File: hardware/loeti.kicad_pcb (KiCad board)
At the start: 4 copper layers, 60 x 80 mm, 62 parts, among them J1 USB_C_Receptacle_USB2.0, J2 20021112-00014T1LF, J3 AudioJack3, Q1 BC817, Q2 BC817, Q3 BC807, Q4 Si4825DDY, DMG4435SSS, IRF939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, SW1 key2, SW2 SW_SPST, SW3 SW_SPST, U1 AP2204R-3.3, U2 STUSB4500QTR, U4 EA_DOGS104B-A, U5 STM32F030K6Tx, U6 ADS1118IDGS, U7 INA301A, U8 ASSR-1218, U9 ASSR-1218

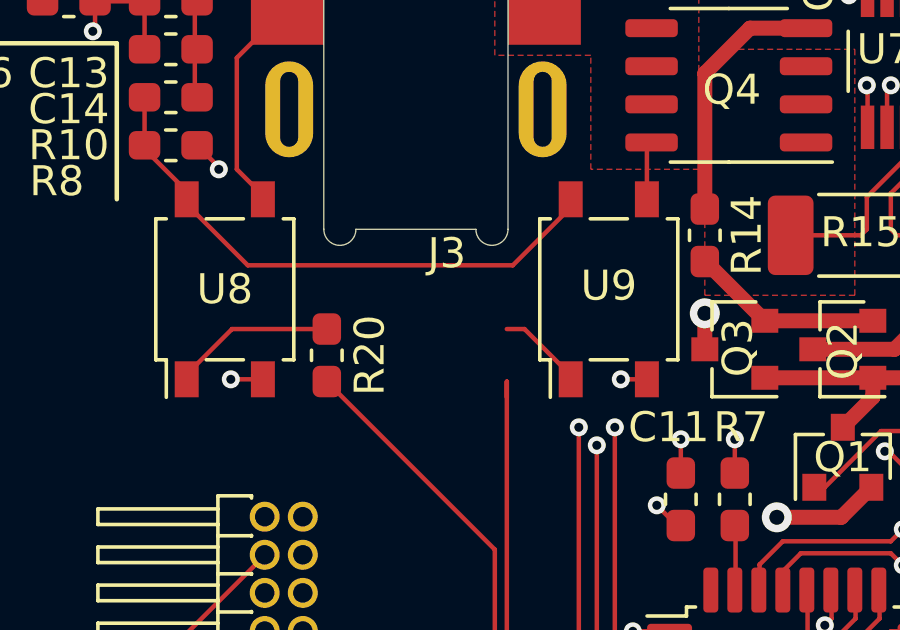
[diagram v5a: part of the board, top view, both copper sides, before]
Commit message: missing footprint
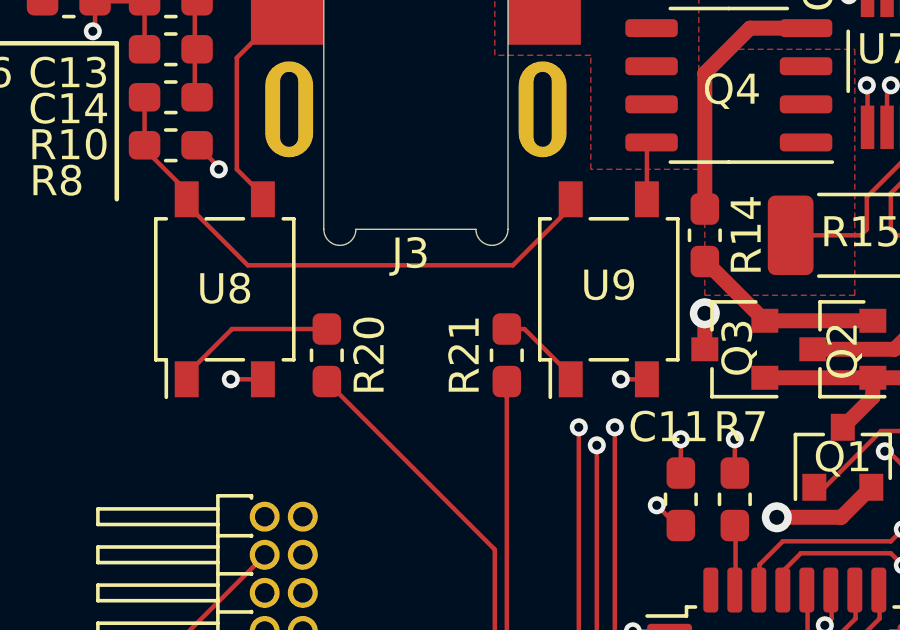
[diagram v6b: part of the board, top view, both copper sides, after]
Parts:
- added R21: 470, Resistor_SMD:R_0603_1608Metric_Pad1.05x0.95mm_HandSolder, F.Cu at (79.4, 58.7)
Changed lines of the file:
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@@
     (tracks 516)
     (zones 0)
-    (modules 62)
+    (modules 63)
     (nets 48)
   )
@@
     (add_net "Net-(C3-Pad2)")
     (add_net "Net-(C4-Pad1)")
+    (add_net "Net-(J1-PadA6)")
+    (add_net "Net-(J1-PadA7)")
+    (add_net "Net-(J1-PadA8)")
+    (add_net "Net-(J1-PadB6)")
+    (add_net "Net-(J1-PadB7)")
+    (add_net "Net-(J1-PadB8)")
+    (add_net "Net-(J2-Pad1)")
+    (add_net "Net-(J2-Pad10)")
+    (add_net "Net-(J2-Pad2)")
+    (add_net "Net-(J2-Pad9)")
     (add_net "Net-(Q1-Pad1)")
     (add_net "Net-(Q1-Pad3)")
@@
     (add_net "Net-(SW2-Pad1)")
     (add_net "Net-(SW3-Pad1)")
+    (add_net "Net-(U2-Pad11)")
+    (add_net "Net-(U2-Pad14)")
+    (add_net "Net-(U2-Pad15)")
+    (add_net "Net-(U2-Pad16)")
+    (add_net "Net-(U2-Pad17)")
+    (add_net "Net-(U2-Pad20)")
+    (add_net "Net-(U2-Pad3)")
+    (add_net "Net-(U2-Pad9)")
+    (add_net "Net-(U4-Pad1)")
+    (add_net "Net-(U4-Pad10)")
+    (add_net "Net-(U4-Pad2)")
+    (add_net "Net-(U4-Pad9)")
+    (add_net "Net-(U5-Pad11)")
+    (add_net "Net-(U5-Pad14)")
+    (add_net "Net-(U6-Pad4)")
+    (add_net "Net-(U6-Pad5)")
     (add_net PD_ALERT_INT)
     (add_net PD_RST)
@@
     (add_net SWCLK)
     (add_net SWDIO)
+    (add_net SWO)
     (add_net T+)
     (add_net VCP_RX)
     (add_net VCP_TX)
+  )
+  (module Resistor_SMD:R_0603_1608Metric_Pad1.05x0.95mm_HandSolder (layer F.Cu)
+    (at 79.4 58.7 270)
+    (descr "Resistor SMD 0603 (1608 Metric), square (rectangular) end terminal, IPC_7351 nominal with elongated pad for handsoldering. (Body size source: http://www.tortai-tech.com/upload/download/2011102023233369053.pdf), generated with kicad-footprint-generator")
+    (tags "resistor handsolder")
+    (attr smd)
+    (fp_text reference R21 (at 0 1.4 90) (layer F.SilkS)
+      (effects (font (size 1 1) (thickness 0.15)))
+    )
+    (fp_text value 470 (at 0 1.43 90) (layer F.Fab)
+      (effects (font (size 1 1) (thickness 0.15)))
+    )
+    (fp_text user %R (at 0 0 90) (layer F.Fab)
+      (effects (font (size 0.4 0.4) (thickness 0.06)))
+    )
+    (fp_line (start 1.65 0.73) (end -1.65 0.73) (layer F.CrtYd) (width 0.05))
+    (fp_line (start 1.65 -0.73) (end 1.65 0.73) (layer F.CrtYd) (width 0.05))
+    (fp_line (start -1.65 -0.73) (end 1.65 -0.73) (layer F.CrtYd) (width 0.05))
+    (fp_line (start -1.65 0.73) (end -1.65 -0.73) (layer F.CrtYd) (width 0.05))
+    (fp_line (start -0.171267 0.51) (end 0.171267 0.51) (layer F.SilkS) (width 0.12))
+    (fp_line (start -0.171267 -0.51) (end 0.171267 -0.51) (layer F.SilkS) (width 0.12))
+    (fp_line (start 0.8 0.4) (end -0.8 0.4) (layer F.Fab) (width 0.1))
+    (fp_line (start 0.8 -0.4) (end 0.8 0.4) (layer F.Fab) (width 0.1))
+    (fp_line (start -0.8 -0.4) (end 0.8 -0.4) (layer F.Fab) (width 0.1))
+    (fp_line (start -0.8 0.4) (end -0.8 -0.4) (layer F.Fab) (width 0.1))
+    (pad 2 smd roundrect (at 0.875 0 270) (size 1.05 0.95) (layers F.Cu F.Paste F.Mask) (roundrect_rratio 0.25)
+      (net 39 SEL_TC_1))
+    (pad 1 smd roundrect (at -0.875 0 270) (size 1.05 0.95) (layers F.Cu F.Paste F.Mask) (roundrect_rratio 0.25)
+      (net 40 "Net-(R21-Pad1)"))
+    (model ${KISYS3DMOD}/Resistor_SMD.3dshapes/R_0603_1608Metric.wrl
+      (at (xyz 0 0 0))
+      (scale (xyz 1 1 1))
+      (rotate (xyz 0 0 0))
+    )
   )
   (module Package_QFP:LQFP-32_7x7mm_P0.8mm (layer F.Cu)
@@
   (module custom:CUI_SJ-3502-SMT (layer F.Cu)
     (at 76.37 47.85 270)
-    (fp_text reference J3 (at 7.45 -1.03) (layer F.SilkS)
+    (fp_text reference J3 (at 7.4627 0.1758) (layer F.SilkS)
       (effects (font (size 1.00148 1.00148) (thickness 0.15)))
     )

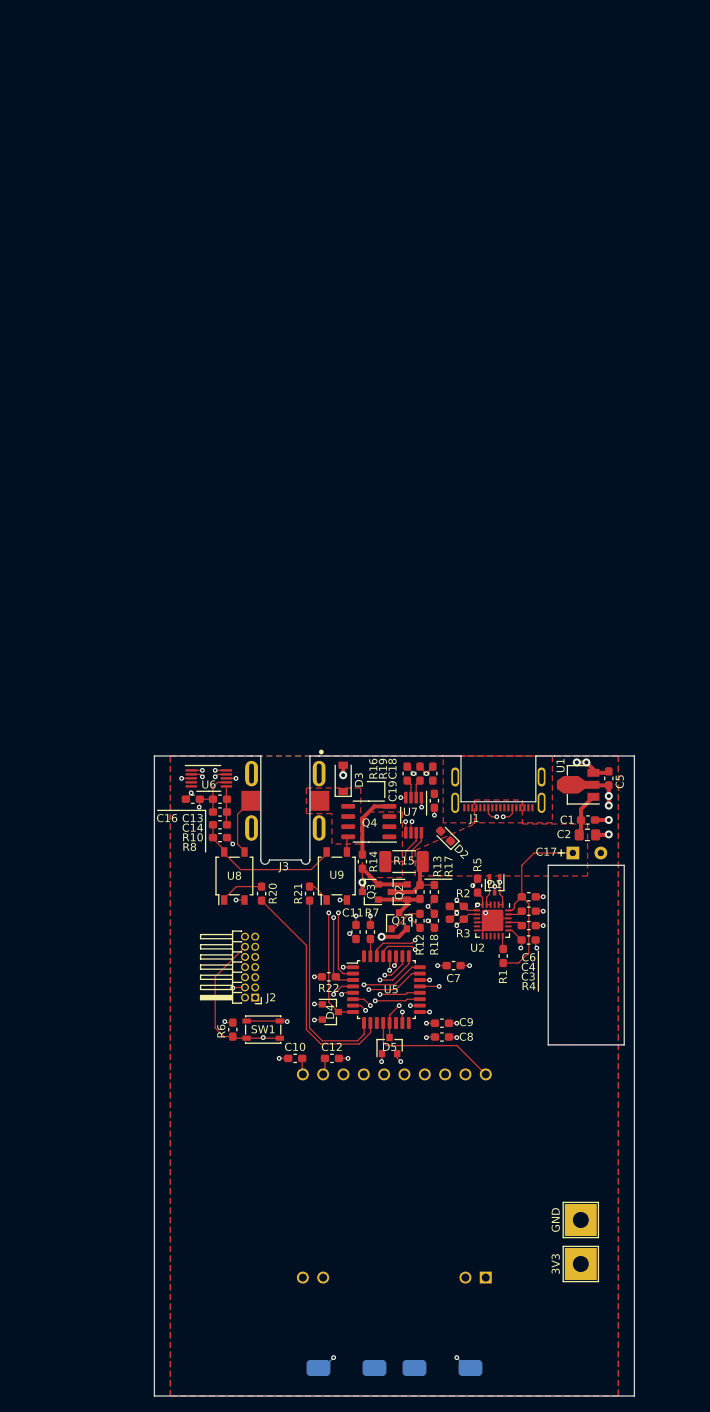
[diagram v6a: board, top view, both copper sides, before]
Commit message: preliminary layout
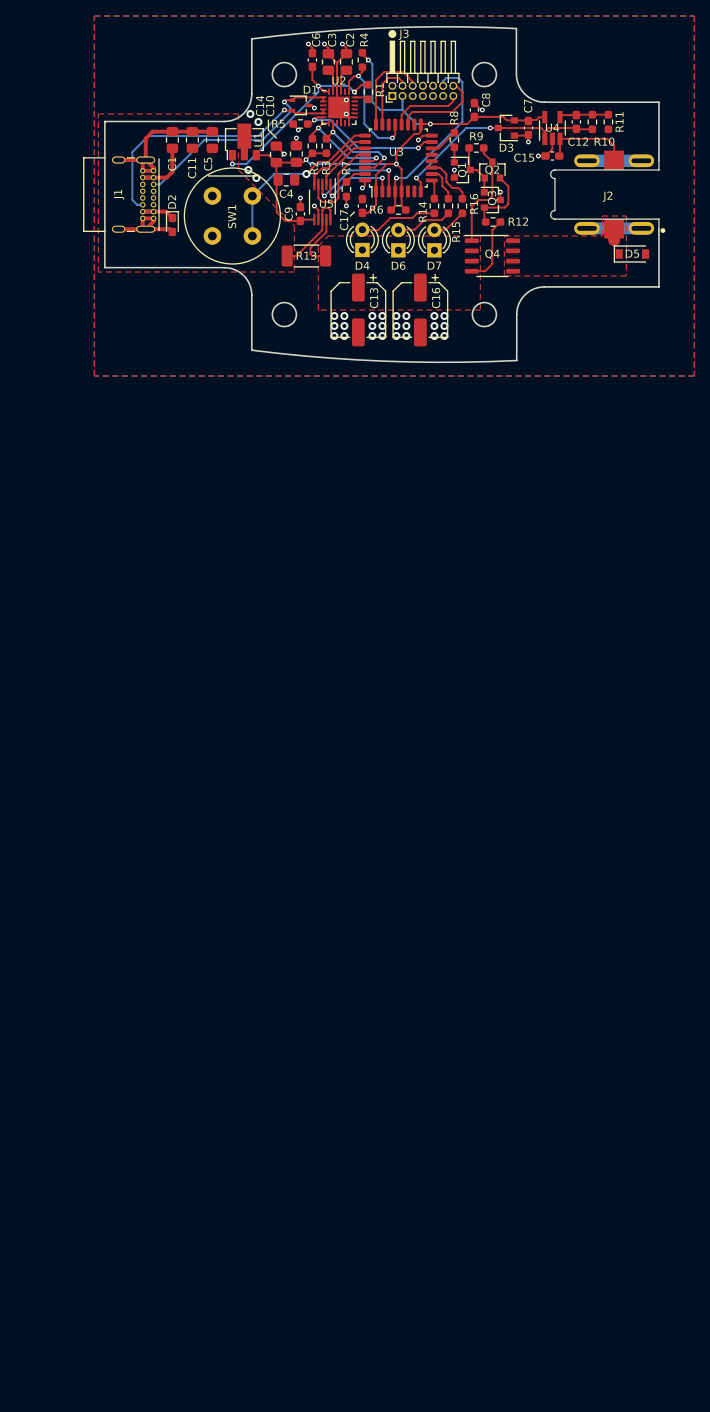
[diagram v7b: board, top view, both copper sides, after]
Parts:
- removed C18, C19: 0.1μF, Capacitor_SMD:C_0603_1608Metric_Pad1.05x0.95mm_HandSolder
- removed R17, R19, R22: 10k, Resistor_SMD:R_0603_1608Metric_Pad1.05x0.95mm_HandSolder
- removed R18: 1k, Resistor_SMD:R_0603_1608Metric_Pad1.05x0.95mm_HandSolder
- removed R20, R21: 470, Resistor_SMD:R_0603_1608Metric_Pad1.05x0.95mm_HandSolder
- removed SW2, SW3: SW_SPST, custom:Omron-B3AL
- removed TP2: GND, TestPoint:TestPoint_THTPad_4.0x4.0mm_Drill2.0mm
- removed TP3: 3V3, TestPoint:TestPoint_THTPad_4.0x4.0mm_Drill2.0mm
- removed U6: ADS1118IDGS, Package_SO:VSSOP-10_3x3mm_P0.5mm
- removed U7: INA301A, Package_SO:VSSOP-8_3.0x3.0mm_P0.65mm
- removed U8, U9: ASSR-1218, Package_SO:SO-4_4.4x4.3mm_P2.54mm
- added C15: 0.1μF, Capacitor_SMD:C_0603_1608Metric_Pad1.08x0.95mm_HandSolder, F.Cu at (109.8, -33.5)
- added D6: LED, LED_THT:LED_D3.0mm, F.Cu at (90.5, -21.7)
- added D7: LED, LED_THT:LED_D3.0mm, F.Cu at (95.0, -21.7)
- added R11: 1k, Resistor_SMD:R_0603_1608Metric_Pad0.98x0.95mm_HandSolder, F.Cu at (116.8, -37.8)
- added R9: 1k, Resistor_SMD:R_0603_1608Metric_Pad0.98x0.95mm_HandSolder, F.Cu at (100.2, -34.5)
- added U3: STM32F030K6Tx, Package_QFP:LQFP-32_7x7mm_P0.8mm, F.Cu at (90.5, -33.2)
- C1, C10, C11, C14, C3, C4, C5: footprint Capacitor_SMD:C_0603_1608Metric_Pad1.05x0.95mm_HandSolder -> Capacitor_SMD:C_0805_2012Metric_Pad1.18x1.45mm_HandSolder
- C12: value 1μF 25V -> 0.1μF; footprint Capacitor_SMD:C_0603_1608Metric_Pad1.05x0.95mm_HandSolder -> Capacitor_SMD:C_0603_1608Metric_Pad1.08x0.95mm_HandSolder
- C13, C16: value 0.1μF -> CP; footprint Capacitor_SMD:C_0603_1608Metric_Pad1.05x0.95mm_HandSolder -> Capacitor_SMD:CP_Elec_6.3x5.9
- C17: value EEU-FR1V471L -> 0.1μF; footprint custom:CP_Radial_D8.0mm_P3.50mm_HOR -> Capacitor_SMD:C_0603_1608Metric_Pad1.08x0.95mm_HandSolder
- C2: value 4.7μF 25V -> 1μF 25V; footprint Capacitor_SMD:C_0805_2012Metric_Pad1.15x1.40mm_HandSolder -> Capacitor_SMD:C_0805_2012Metric_Pad1.18x1.45mm_HandSolder
- C6, C7, C8, C9: footprint Capacitor_SMD:C_0603_1608Metric_Pad1.05x0.95mm_HandSolder -> Capacitor_SMD:C_0603_1608Metric_Pad1.08x0.95mm_HandSolder
- D3: value D_Schottky -> BAT54S; footprint Diode_SMD:D_SOD-123 -> Package_TO_SOT_SMD:SOT-23
- D4: value BAT54S -> LED; footprint Package_TO_SOT_SMD:SOT-23 -> LED_THT:LED_D3.0mm
- D5: value BAT54S -> D_Schottky; footprint Package_TO_SOT_SMD:SOT-23 -> Diode_SMD:D_SOD-123
- J1: footprint custom:CX90M-16P -> Connector_USB:USB_C_Receptacle_GCT_USB4085
- J2: value 20021112-00014T1LF -> AudioJack3; footprint Connector_PinHeader_1.27mm:PinHeader_2x07_P1.27mm_Horizontal -> custom:CUI_SJ-3502-SMT
- J3: value AudioJack3 -> 20021112-00014T1LF; footprint custom:CUI_SJ-3502-SMT -> Connector_PinHeader_1.27mm:PinHeader_2x07_P1.27mm_Horizontal
- R1, R2, R3, R4, R5, R6, R7: footprint Resistor_SMD:R_0603_1608Metric_Pad1.05x0.95mm_HandSolder -> Resistor_SMD:R_0603_1608Metric_Pad0.98x0.95mm_HandSolder
- R10: value 47 -> 220k; footprint Resistor_SMD:R_0603_1608Metric_Pad1.05x0.95mm_HandSolder -> Resistor_SMD:R_0603_1608Metric_Pad0.98x0.95mm_HandSolder
- R12: value 1k -> 20; footprint Resistor_SMD:R_0603_1608Metric_Pad1.05x0.95mm_HandSolder -> Resistor_SMD:R_0603_1608Metric_Pad0.98x0.95mm_HandSolder
- R13: value 1k -> WSLP2010R0100FEA; footprint Resistor_SMD:R_0603_1608Metric_Pad1.05x0.95mm_HandSolder -> Resistor_SMD:R_2010_5025Metric_Pad1.40x2.65mm_HandSolder
- R14: value 20 -> 1k; footprint Resistor_SMD:R_0603_1608Metric_Pad1.05x0.95mm_HandSolder -> Resistor_SMD:R_0603_1608Metric_Pad0.98x0.95mm_HandSolder
- R15: value WSLP2010R0100FEA -> 1k; footprint Resistor_SMD:R_2010_5025Metric_Pad1.52x2.65mm_HandSolder -> Resistor_SMD:R_0603_1608Metric_Pad0.98x0.95mm_HandSolder
- R16: value 25k -> 1k; footprint Resistor_SMD:R_0603_1608Metric_Pad1.05x0.95mm_HandSolder -> Resistor_SMD:R_0603_1608Metric_Pad0.98x0.95mm_HandSolder
- R8: value 1M -> 1k; footprint Resistor_SMD:R_0603_1608Metric_Pad1.05x0.95mm_HandSolder -> Resistor_SMD:R_0603_1608Metric_Pad0.98x0.95mm_HandSolder
- SW1: value key2 -> D6R; footprint Button_Switch_SMD:SW_SPST_PTS810 -> custom:D6R
- U4: value EA_DOGS104B-A -> TLV333-DBV; footprint Display:EA_DOGS104X-A -> Package_TO_SOT_SMD:SOT-23-5_HandSoldering; moved to F.Cu
- U5: value STM32F030K6Tx -> INA239; footprint Package_QFP:LQFP-32_7x7mm_P0.8mm -> Package_SO:VSSOP-10_3x3mm_P0.5mm
- moved U4 143.9 mm to (109.8, -37.0)
- moved C12 121.0 mm to (112.8, -37.8), turned to 90 degrees
- moved C8 115.9 mm to (100.0, -39.2), turned to 90 degrees
- moved C10 113.1 mm to (77.8, -33.8), turned to 90 degrees
- moved R4 111.9 mm to (86.0, -45.5), turned to 90 degrees
- moved C3 110.8 mm to (81.8, -45.2), turned to 90 degrees
- moved J2 109.6 mm to (116.7, -28.7)
- moved R1 109.3 mm to (86.8, -41.5), turned to 90 degrees
- moved C6 108.0 mm to (79.8, -45.5), turned to 270 degrees
- moved C7 105.1 mm to (106.8, -37.0), turned to 270 degrees
- moved R6 104.5 mm to (90.5, -26.8), turned to 180 degrees
- moved D5 103.5 mm to (119.8, -21.2), turned to 0 degrees
- moved U2 103.4 mm to (83.1, -39.6), turned to 0 degrees
- moved C9 102.7 mm to (78.2, -26.2), turned to 90 degrees
- moved SW1 101.8 mm to (69.8, -26.0), turned to 270 degrees
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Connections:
- C10 pad 1: Net-(C10-Pad1) -> +3V3
- C11 pad 1: +3V3 -> SHUNT+
- C12 pad 1: +3V3 -> ADC_IN2
- C12 pad 2: HEATER- -> Net-(C12-Pad2)
- C13 pad 1: HEATER- -> SHUNT-
- C13 pad 2: Net-(C13-Pad2) -> HEATER-
- C14 pad 1: HEATER- -> +3V3
- C14 pad 2: Net-(C13-Pad2) -> HEATER-
- C16 pad 1: +3V3 -> SHUNT-
- C17 pad 1: SHUNT+ -> +3V3
- C2 pad 1: SHUNT+ -> HEATER-
- C2 pad 2: HEATER- -> Net-(C2-Pad2)
- C3 pad 1: HEATER- -> Net-(C3-Pad1)
- C3 pad 2: Net-(C3-Pad2) -> HEATER-
- C4 pad 1: Net-(C4-Pad1) -> +3V3
- C5 pad 1: +3V3 -> SHUNT+
- D3 pad 1: HEATER+ -> HEATER-
- D3 pad 2: HEATER- -> +3V3
- D4 pad 2: +3V3 -> Net-(D4-Pad2)
- D5 pad 1: HEATER- -> HEATER+
- D5 pad 2: +3V3 -> HEATER-
- Q2 pad 3: SHUNT+ -> SHUNT-
- R10 pad 1: Net-(R10-Pad1) -> ADC_IN2
- R10 pad 2: Net-(C13-Pad2) -> Net-(C12-Pad2)
- R12 pad 1: PWM -> Net-(Q2-Pad2)
- R12 pad 2: Net-(Q1-Pad1) -> Net-(Q4-Pad4)
- R13 pad 1: Net-(Q1-Pad3) -> SHUNT+
- R13 pad 2: SHUNT+ -> SHUNT-
- R14 pad 1: Net-(Q2-Pad2) -> Net-(D4-Pad2)
- R14 pad 2: Net-(Q4-Pad4) -> LED0
- R15 pad 1: SHUNT+ -> Net-(D6-Pad2)
- R15 pad 2: SHUNT- -> LED1
- R16 pad 1: HEATER- -> Net-(D7-Pad2)
- R16 pad 2: CUR_LIMIT -> LED2
- R8 pad 1: Net-(R10-Pad1) -> PWM
- R8 pad 2: +3V3 -> Net-(Q1-Pad1)
- SW1 pad 1: NRST -> SW
- SW1 pad 2: HEATER- -> SW
- U2 pad 21: Net-(C3-Pad2) -> Net-(C2-Pad2)
- U2 pad 23: Net-(C4-Pad1) -> Net-(C3-Pad1)
- U4 pad 1: (no net) -> ADC_IN2
- U4 pad 2: (no net) -> HEATER-
- U5 pad 1: +3V3 -> CURR_CS
- U5 pad 10: SEL_TC_0 -> SHUNT+
- U5 pad 2: CUR_RESET -> SPI1_MISO
- U5 pad 3: CUR_NALERT -> CURR_ALERT
- U5 pad 4: NRST -> SPI1_MOSI
- U5 pad 5: +3V3 -> SPI1_SCK
- U5 pad 6: Net-(SW2-Pad1) -> +3V3
- U5 pad 7: Net-(SW3-Pad1) -> HEATER-
- U5 pad 8: ADC_IN2 -> SHUNT+
- U5 pad 9: SEL_TC_1 -> SHUNT-
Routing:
- net +3V3: track 28.5 -> 87.4 mm, vias 20 -> 4
- net SPI1_SCK: track 64.4 -> 9.14 mm, vias 2 -> 0
- net Net-(SW2-Pad1): track 53.2 -> 0.00 mm, vias 2 -> 0
- net SPI1_MISO: track 59.2 -> 7.30 mm, vias 2 -> 0
- net Net-(SW3-Pad1): track 49.3 -> 0.00 mm, vias 2 -> 0
- net SPI1_NSS1: track 44.7 -> 0.00 mm, vias 2 -> 0
- net SPI1_MOSI: track 55.3 -> 11.9 mm, vias 2 -> 0
- net SEL_TC_0: track 29.0 -> 0.00 mm
- net CUR_NALERT: track 28.3 -> 0.00 mm, vias 2 -> 0
- net HEATER-: track 56.2 -> 82.9 mm, vias 30 -> 47
- net CUR_RESET: track 26.0 -> 0.00 mm, vias 2 -> 0
- net SEL_TC_1: track 25.7 -> 0.00 mm
- net SW: track 0.00 -> 22.2 mm, vias 0 -> 1
- net ADC_IN7: track 21.7 -> 0.00 mm, vias 2 -> 0
- net SWDIO: track 28.8 -> 8.60 mm, vias 2 -> 0
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- removed copper zone on In1.Cu, net +3V3
- removed copper zone on In2.Cu, net HEATER-
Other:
- board size 60 x 80 mm -> 69.3 x 41.9 mm
- copper layers 4 -> 2
- board text added: "Löti mini"
- board text added: "af 2021 v0.1"
- board text removed: "Löti"
- board text removed: "af 2020"
- board text removed: "hawki edition"
- board text removed: "v4"

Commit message: production version, v5
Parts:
- removed the C10 at (77.8, -33.8)
- removed the C14 at (75.2, -33.7)
- removed the C5 at (67.2, -35.5)
- removed the R12 at (102.3, -25.2)
- removed the R8 at (97.5, -35.5)
- added D11: BZX84Cxx, Package_TO_SOT_SMD:TSOT-23_HandSoldering, F.Cu at (101.2, -38.0)
- added D4: BAS16W, Package_TO_SOT_SMD:SOT-323_SC-70_Handsoldering, F.Cu at (83.5, -25.5)
- added D8: BAS16W, Package_TO_SOT_SMD:SOT-323_SC-70_Handsoldering, F.Cu at (115.0, -37.5)
- added D9: BAS16W, Package_TO_SOT_SMD:SOT-323_SC-70_Handsoldering, F.Cu at (121.5, -37.5)
- added R13: 1k, Resistor_SMD:R_0603_1608Metric_Pad0.98x0.95mm_HandSolder, F.Cu at (100.0, -30.5)
- added R14: 25k, Resistor_SMD:R_0603_1608Metric_Pad0.98x0.95mm_HandSolder, F.Cu at (98.0, -22.5)
- added R15: 1k, Resistor_SMD:R_0603_1608Metric_Pad0.98x0.95mm_HandSolder, F.Cu at (103.5, -32.5)
- added R16: 1M, Resistor_SMD:R_0603_1608Metric_Pad0.98x0.95mm_HandSolder, F.Cu at (110.5, -34.2)
- added R17: 10k, Resistor_SMD:R_0603_1608Metric_Pad0.98x0.95mm_HandSolder, F.Cu at (118.2, -38.2)
- added R20: 20, Resistor_SMD:R_0603_1608Metric_Pad0.98x0.95mm_HandSolder, F.Cu at (108.0, -23.8)
- added R23: 10k, Resistor_SMD:R_0603_1608Metric_Pad0.98x0.95mm_HandSolder, F.Cu at (104.2, -40.8)
- added R24: 10k, Resistor_SMD:R_0603_1608Metric_Pad0.98x0.95mm_HandSolder, F.Cu at (108.0, -29.8)
- added R6: 10k, Resistor_SMD:R_0603_1608Metric_Pad0.98x0.95mm_HandSolder, F.Cu at (89.2, -21.2)
- added R7: 1k, Resistor_SMD:R_0603_1608Metric_Pad0.98x0.95mm_HandSolder, F.Cu at (91.8, -22.2)
- added U4: 74AHC1G08, Package_TO_SOT_SMD:SOT-353_SC-70-5_Handsoldering, F.Cu at (101.5, -34.8)
- added U6: TMP100, Package_TO_SOT_SMD:SOT-23-6_Handsoldering, F.Cu at (84.5, -34.2)
- C10: renamed from C9; value 0.1μF -> 100n
- C11: value 1μF 25V -> 100n; footprint Capacitor_SMD:C_0805_2012Metric_Pad1.18x1.45mm_HandSolder -> Capacitor_SMD:C_0603_1608Metric_Pad1.08x0.95mm_HandSolder
- C12: renamed from C15; value 0.1μF -> 100n
- C13: renamed from C12; value 0.1μF -> 100n
- C14: renamed from C17; value 0.1μF -> 100n
- C3: renamed from C2; value 1μF 25V -> 1u
- C4: renamed from C3; value 1μF 25V -> 1u
- C5: renamed from C1; value 1μF 25V -> 4.7u
- C6: value 0.1μF -> 100n
- C7: renamed from C4; value 1μF 25V -> 4.7u
- C8: renamed from C7; value 0.1μF -> 100n
- C9: renamed from C8; value 0.1μF -> 100n
- D1: footprint Package_TO_SOT_SMD:SOT-323_SC-70 -> Package_TO_SOT_SMD:SOT-323_SC-70_Handsoldering
- D3: value BAT54S -> BAS16W; footprint Package_TO_SOT_SMD:SOT-23 -> Package_TO_SOT_SMD:SOT-323_SC-70_Handsoldering
- D5: renamed from D4; footprint LED_THT:LED_D3.0mm -> LED_THT:LED_D1.8mm_W3.3mm_H2.4mm
- D6, D7: footprint LED_THT:LED_D3.0mm -> LED_THT:LED_D1.8mm_W3.3mm_H2.4mm
- J1: value USB_C_Receptacle_USB2.0 -> GCT USB4105; footprint Connector_USB:USB_C_Receptacle_GCT_USB4085 -> Connector_USB:USB_C_Receptacle_HRO_TYPE-C-31-M-12
- Q1, Q2, Q3: footprint Package_TO_SOT_SMD:SOT-23 -> Package_TO_SOT_SMD:SOT-23_Handsoldering
- R10: renamed from R14; value 1k -> 10k
- R11: renamed from R15; value 1k -> 10k
- R12: renamed from R16; value 1k -> 10k
- R18: renamed from R9; value 1k -> 10k
- U2: renamed from U1; footprint Package_TO_SOT_SMD:SOT-89-3 -> Package_TO_SOT_SMD:SOT-89-3_Handsoldering
- U5: value INA239 -> INA301; footprint Package_SO:VSSOP-10_3x3mm_P0.5mm -> Package_SO:VSSOP-8_3.0x3.0mm_P0.65mm
- moved C11 35.9 mm to (100.0, -28.8), turned to 0 degrees
- moved D7 29.6 mm to (80.5, -47.5), turned to 270 degrees
- moved D6 26.7 mm to (83.8, -47.5), turned to 270 degrees
- moved D5 25.8 mm to (87.0, -47.5), turned to 270 degrees
- moved R19 23.9 mm to (102.8, -18.8)
- moved C10 22.6 mm to (100.0, -32.5), turned to 180 degrees
- moved C14 22.3 mm to (107.1, -34.2), turned to 180 degrees
- moved U5 22.1 mm to (102.5, -22.5), turned to 0 degrees
- moved R12 21.0 mm to (83.5, -42.0), turned to 270 degrees
- moved D3 20.9 mm to (86.5, -25.5), turned to 90 degrees
- moved C8 20.8 mm to (89.0, -26.2)
- moved R11 18.7 mm to (85.2, -42.0), turned to 270 degrees
- moved R10 16.8 mm to (87.0, -42.0), turned to 270 degrees
- moved C9 15.0 mm to (92.5, -26.2), turned to 270 degrees
- moved C6 14.4 mm to (74.0, -32.2), turned to 0 degrees
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- renumbered C13 to C1, C16 to C2, D5 to D10, R13 to R19, R10 to R21, R11 to R22, R7 to R8, R6 to R9, U2 to U1, U4 to U7
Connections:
- C1 pad 1: SHUNT- -> SHUNT+
- C11 pad 1: SHUNT+ -> ADC_IN1
- C13 pad 1: ADC_IN2 -> Net-(C13-Pad1)
- C2 pad 1: SHUNT- -> SHUNT+
- D3 pad 1: HEATER- -> ADC_IN3
- D3 pad 2: +3V3 -> (no net)
- D3 pad 3: ADC_IN2 -> +3V3
- Q2 pad 3: SHUNT- -> SHUNT+
- R18 pad 2: SHUNT- -> SHUNT+
- R21 pad 1: ADC_IN2 -> Net-(C13-Pad1)
- U3 pad 10: LED1 -> (no net)
- U3 pad 11: LED2 -> (no net)
- U3 pad 13: (no net) -> CURR_ALERT
- U3 pad 2: CURR_CS -> SW
- U3 pad 25: SW -> LED0
- U3 pad 26: SPI1_SCK -> LED1
- U3 pad 27: SPI1_MISO -> LED2
- U3 pad 28: SPI1_MOSI -> (no net)
- U3 pad 3: CURR_ALERT -> (no net)
- U3 pad 6: (no net) -> CURR_RESET
- U3 pad 7: (no net) -> ADC_IN1
- U3 pad 9: LED0 -> ADC_IN3
- U5 pad 1: CURR_CS -> +3V3
- U5 pad 2: SPI1_MISO -> Net-(R13-Pad2)
- U5 pad 3: CURR_ALERT -> Net-(R14-Pad2)
- U5 pad 4: SPI1_MOSI -> HEATER-
- U5 pad 5: SPI1_SCK -> CURR_RESET
- U5 pad 6: +3V3 -> CURR_ALERT
- U5 pad 7: HEATER- -> SHUNT-
- U7 pad 1: ADC_IN2 -> Net-(C13-Pad1)
- U7 pad 3: T+ -> Net-(D8-Pad1)
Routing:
- net +3V3: track 87.4 -> 12.9 mm, vias 4 -> 1
- net ADC_IN3: track 0.00 -> 24.7 mm, vias 0 -> 2
- net CURR_RESET: track 0.00 -> 18.7 mm, vias 0 -> 2
- net HEATER-: track 82.9 -> 65.7 mm, vias 47 -> 66
- net Net-(D8-Pad1): track 0.00 -> 15.7 mm
- net ADC_IN2: track 27.8 -> 15.0 mm
- net SHUNT-: track 21.0 -> 8.60 mm
- net SPI1_MOSI: track 11.9 -> 0.00 mm
- net Net-(C13-Pad1): track 0.00 -> 10.8 mm
- net Net-(R13-Pad2): track 0.00 -> 10.7 mm, vias 0 -> 2
- net CURR_CS: track 10.4 -> 0.00 mm, vias 2 -> 0
- net CURR_ALERT: track 13.6 -> 23.8 mm
- net CC2: track 34.3 -> 24.7 mm, vias 1 -> 2
- net SPI1_SCK: track 9.14 -> 0.00 mm
- net Net-(D5-Pad2): track 9.86 -> 2.05 mm
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- added copper zone on F.Cu, net +3V3
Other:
- net class Default: clearance 0.15 -> 0.127; trace_width 0.15 -> 0.25
- rule trace_clearance: 0.15 -> 0.127
- rule trace_min: 0.1 -> 0.127
- board text added: "*"
- board text added: "af 2021 v5"
- board text added: "löti"
- board text removed: "Löti mini"
- board text removed: "af 2021 v0.1"
